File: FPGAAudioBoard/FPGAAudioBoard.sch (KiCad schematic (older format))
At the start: 1 part

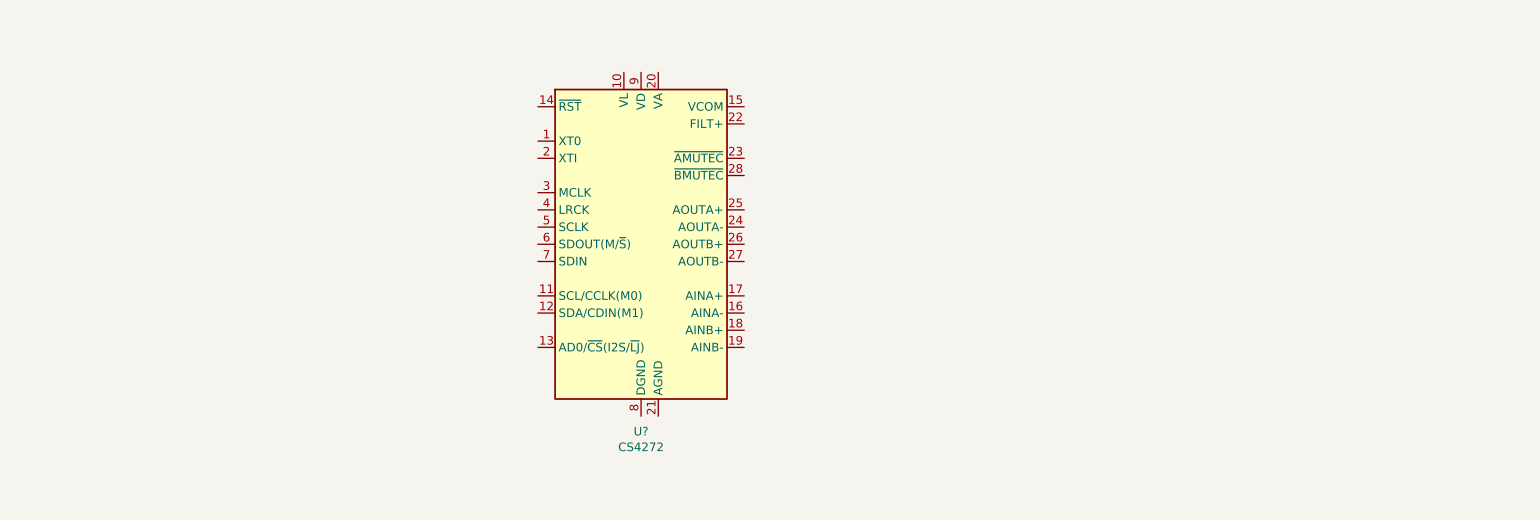
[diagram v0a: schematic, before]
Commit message: Added audio codec, PMOD connector and XLR
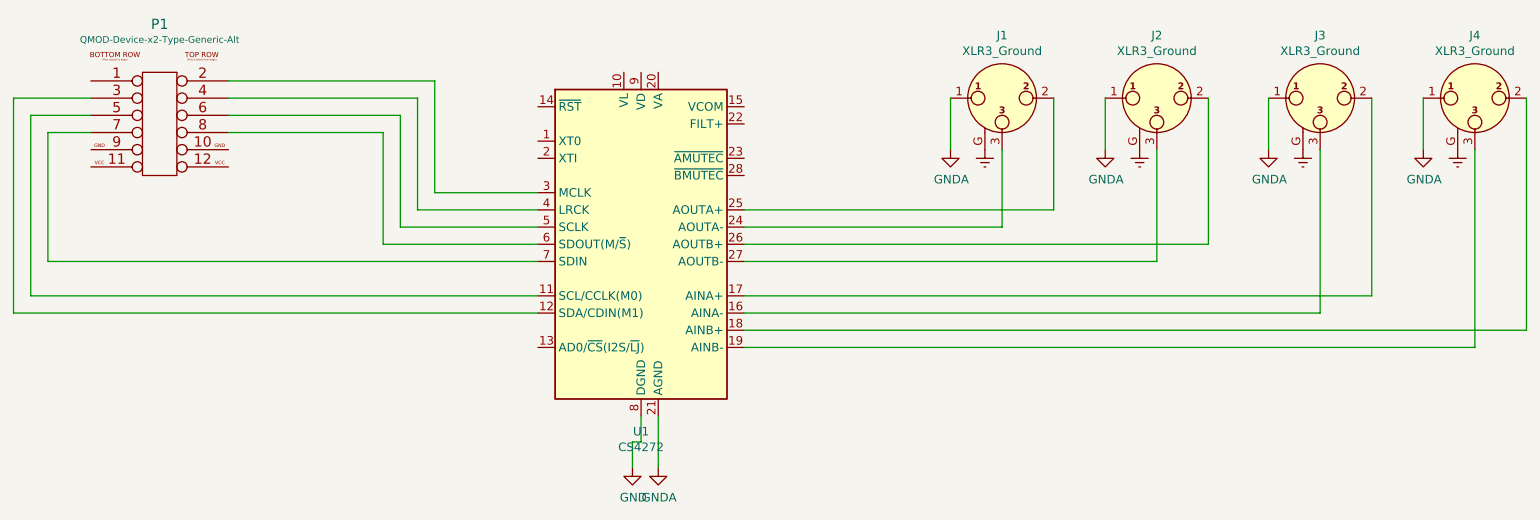
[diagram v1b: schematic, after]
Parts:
- added J1, J2, J3, J4: XLR3_Ground, Connector_Audio:Jack_XLR_Neutrik_NC3FAH_Horizontal, symbol Connector:XLR3_Ground
- added P1: QMOD-Device-x2-Type-Generic-Alt, pmod-conn_6x2:pmod_pin_array_6x2, symbol pmod:QMOD-Device-x2-Type-Generic-Alt
- gave numbers to parts that had none: 1
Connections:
- net at U1.11 (SCL/CCLK(M0)): now also P1.5 (P9)
- net at U1.12 (SDA/CDIN(M1)): now also P1.3 (P8)
- net at U1.16 (AINA-): now also J3.3
- net at U1.17 (AINA+): now also J3.2
- net at U1.18 (AINB+): now also J4.2
- net at U1.19 (AINB-): now also J4.3
- net GNDA: now reaches U1.21 (AGND)
- net GNDA: now also J1.1, J2.1, J3.1, J4.1
- net at U1.24 (AOUTA-): now also J1.3
- net at U1.25 (AOUTA+): now also J1.2
- net at U1.26 (AOUTB+): now also J2.2
- net at U1.27 (AOUTB-): now also J2.3
- net at U1.3 (MCLK): now also P1.2 (P1)
- net at U1.4 (LRCK): now also P1.4 (P2)
- net at U1.5 (SCLK): now also P1.6 (P3)
- net at U1.6 (SDOUT(M/~S~)): now also P1.8 (10)
- net at U1.7 (SDIN): now also P1.7 (P10)
- net GND: now reaches U1.8 (DGND)
- new net Earth: J1.G, J2.G, J3.G, J4.G

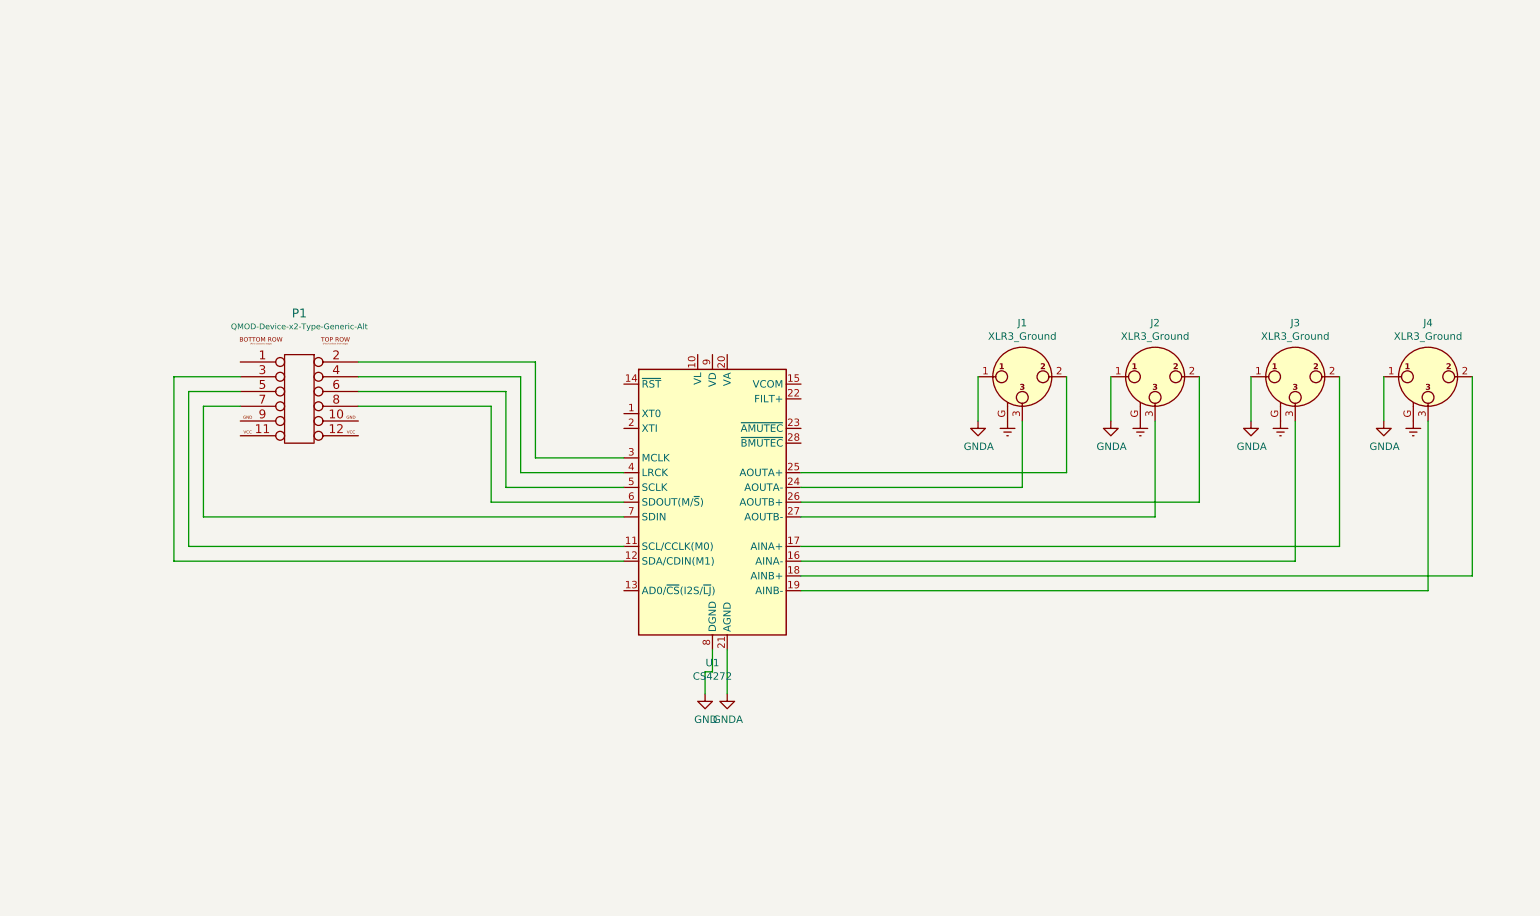
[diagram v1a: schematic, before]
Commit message: Added opamps, configuration R
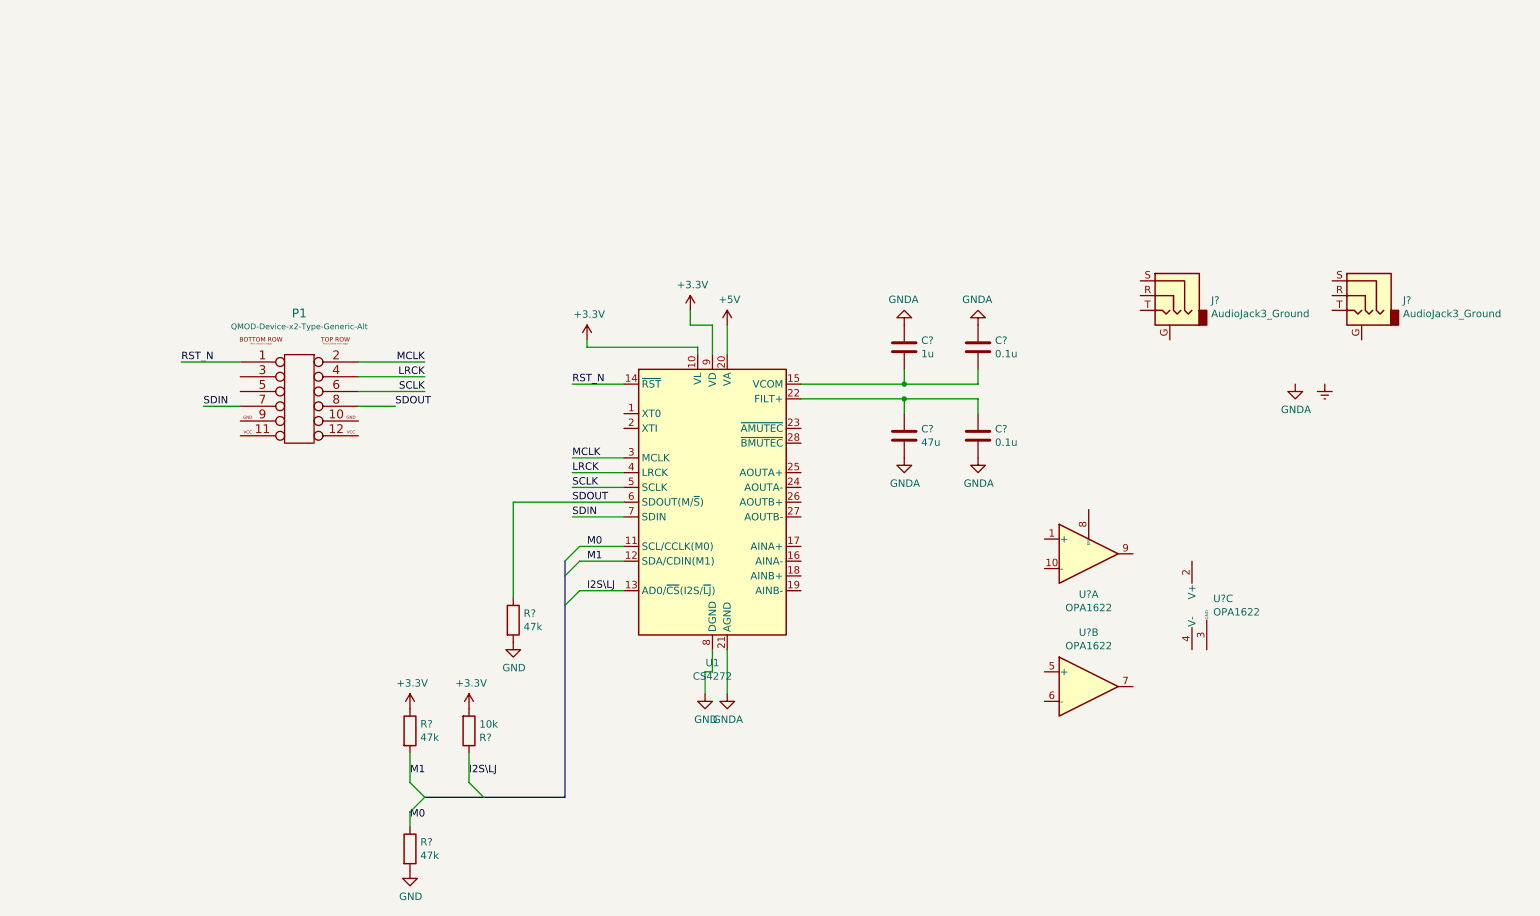
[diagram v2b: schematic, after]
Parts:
- removed J1, J2, J3, J4: XLR3_Ground, Connector_Audio:Jack_XLR_Neutrik_NC3FAH_Horizontal, symbol Connector:XLR3_Ground
- added C?: 47u, symbol Device:C
- added C? (x2): 0.1u, symbol Device:C
- added C?: 1u, symbol Device:C
- added J? (x2): AudioJack3_Ground, symbol Connector:AudioJack3_Ground
- added R? (x3): 47k, symbol Device:R
- added R?: 10k, symbol Device:R
- added U? (x3): OPA1622, Package_SON:Texas_S-PVSON-N10, symbol Amplifier_Audio:OPA1622
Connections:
- net GND: now also R?.2, R?.2
- net GNDA: now also C?.1, C?.1, C?.2, C?.2
- net +3V3: now reaches U1.10 (VL)
- net +3V3: now also U1.9 (VD), R?.1, R?.2
- net at P1.5 (P9): no longer U1.11 (SCL/CCLK(M0))
- net at P1.3 (P8): no longer U1.12 (SDA/CDIN(M1))
- net I2S\LJ: now reaches U1.13 (AD0/~CS~(I2S/~LJ~))
- net I2S\LJ: now also R?.1
- net RST_N: now reaches U1.14 (~RST)
- net RST_N: now also P1.1 (P7)
- net at U1.15 (VCOM): now also C?.2, C?.2
- net +5V: now reaches U1.20 (VA)
- net at U1.22 (FILT+): now also C?.1, C?.1
- net MCLK: now reaches P1.2 (P1), U1.3 (MCLK)
- net LRCK: now reaches P1.4 (P2), U1.4 (LRCK)
- net SCLK: now reaches P1.6 (P3), U1.5 (SCLK)
- net SDOUT: now reaches P1.8 (10), U1.6 (SDOUT(M/~S~))
- net SDOUT: now also R?.1
- net SDIN: now reaches P1.7 (P10), U1.7 (SDIN)
- new net: U?.11 (V-), U?.4 (V-)
- new net M0: R?.1, U1.11 (SCL/CCLK(M0))
- new net M1: R?.2, U1.12 (SDA/CDIN(M1))

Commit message: Minor changes :)
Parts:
- added U? (x6): OPA1622, Package_SON:Texas_S-PVSON-N10, symbol Amplifier_Audio:OPA1622
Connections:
- new net: U?.11 (V-), U?.4 (V-) (x2)
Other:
- moved on the sheet: C?, P1, R?, U1, U?A, U?B, U?C
